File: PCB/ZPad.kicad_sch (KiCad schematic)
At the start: 19 parts, among them J1 Conn_01x04, SW1 SW_Push, SW2 SW_Push, SW3 SW_Push, SW4 SW_Push, SW5 SW_Push, SW6 SW_Push, SW7 SW_Push, SW8 SW_Push, SW9 RotaryEncoder_Switch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

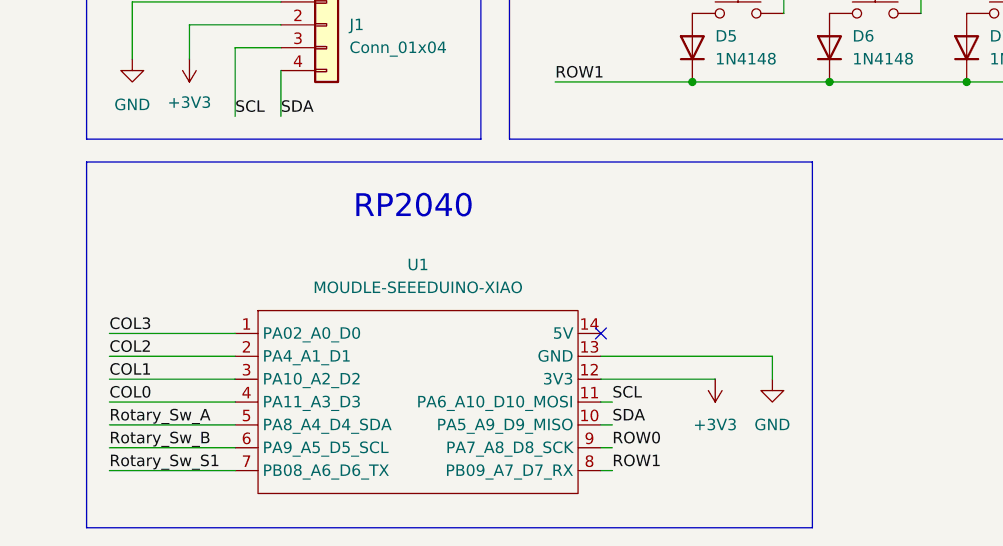
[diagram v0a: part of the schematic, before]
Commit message: Fixed stuff according to reviewer
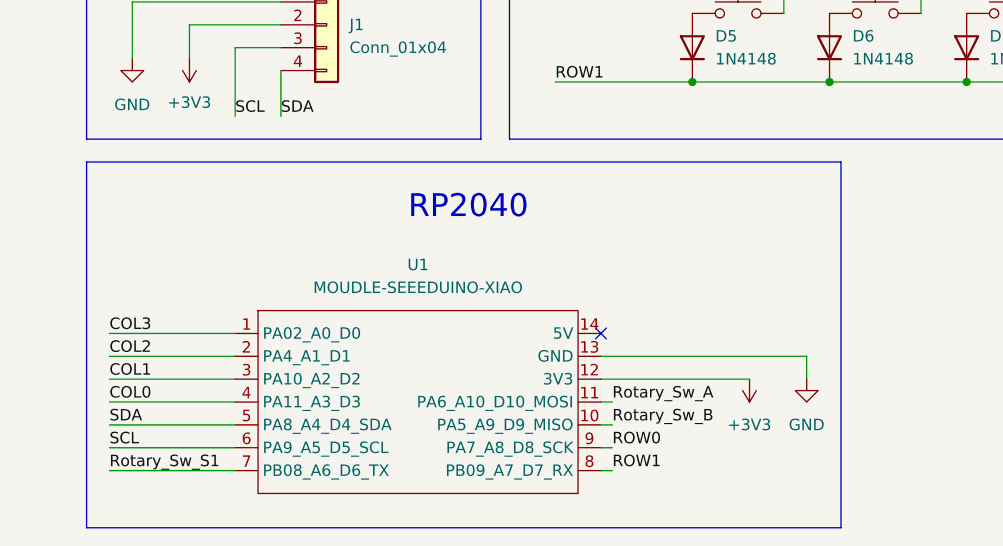
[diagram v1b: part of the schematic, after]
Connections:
- net Rotary_Sw_A: now also U1.11 (PA6_A10_D10_MOSI); no longer U1.5 (PA8_A4_D4_SDA)
- net Rotary_Sw_B: now also U1.10 (PA5_A9_D9_MISO); no longer U1.6 (PA9_A5_D5_SCL)
- net SCL: now also U1.6 (PA9_A5_D5_SCL); no longer U1.11 (PA6_A10_D10_MOSI)
- net SDA: now also U1.5 (PA8_A4_D4_SDA); no longer U1.10 (PA5_A9_D9_MISO)
